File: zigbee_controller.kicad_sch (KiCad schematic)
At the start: 83 parts, among them J1 Terminal MKDS, J10 Terminal MKDS, J11 Terminal MKDS, J12 Terminal MKDS, J13 Terminal MKDS, J2 Conn_01x02, J3 Conn_01x06, J4 Conn_01x07, J5 Conn_01x05, P1 USB_C_Receptacle_GCT_USB4105, Q2 IRLB3813, Q3 IRLB3813, Q4 IRLB3813, Q5 IRLB3813, Q6 IRLB3813, SW2 EN, SW4 Boot, U1 TPS54560, U2 ESP32-C6-MINI-1, U4 TC4427, U5 TC4427, U6 RT9080, U9 CH224K

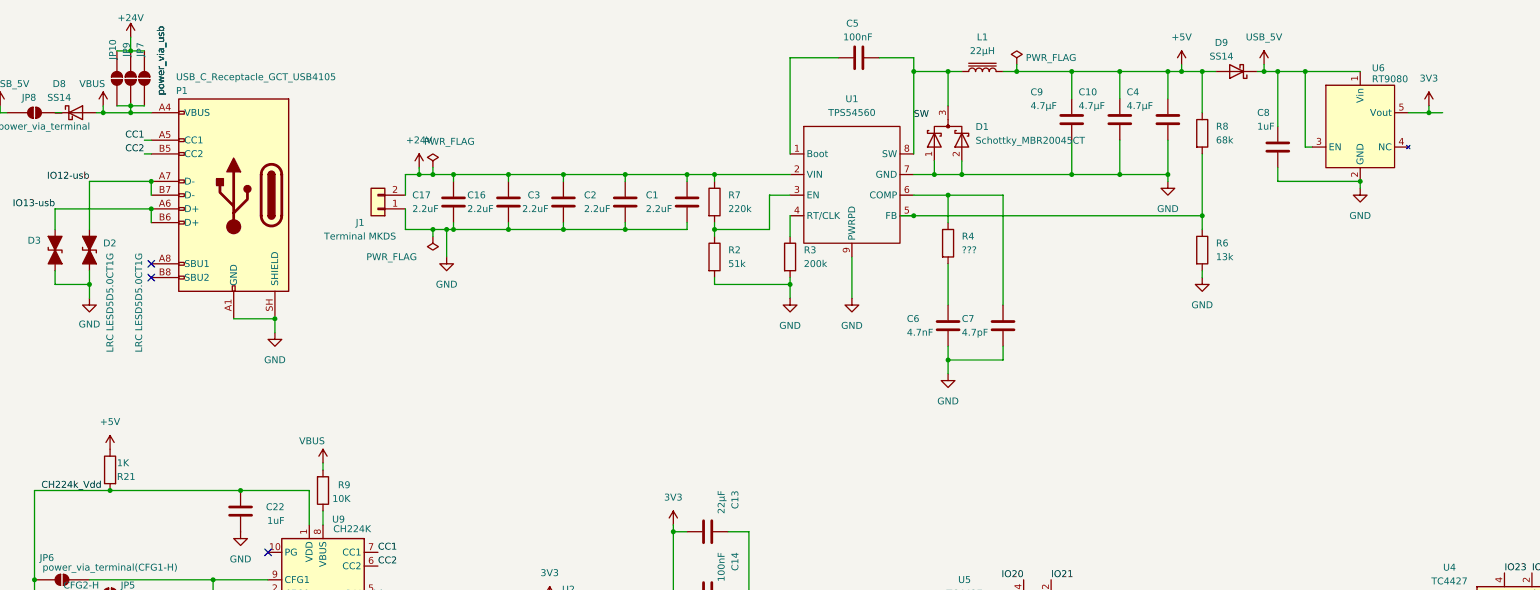
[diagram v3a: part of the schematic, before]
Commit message: USB power, all checks pass
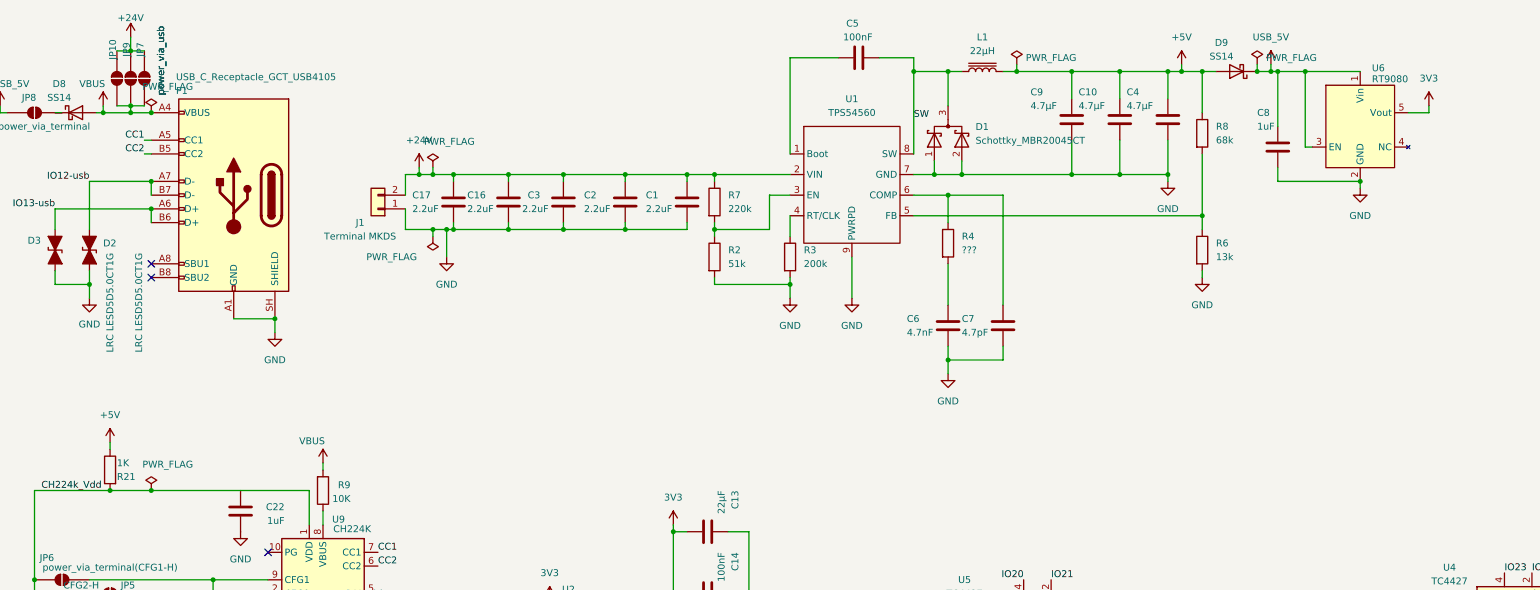
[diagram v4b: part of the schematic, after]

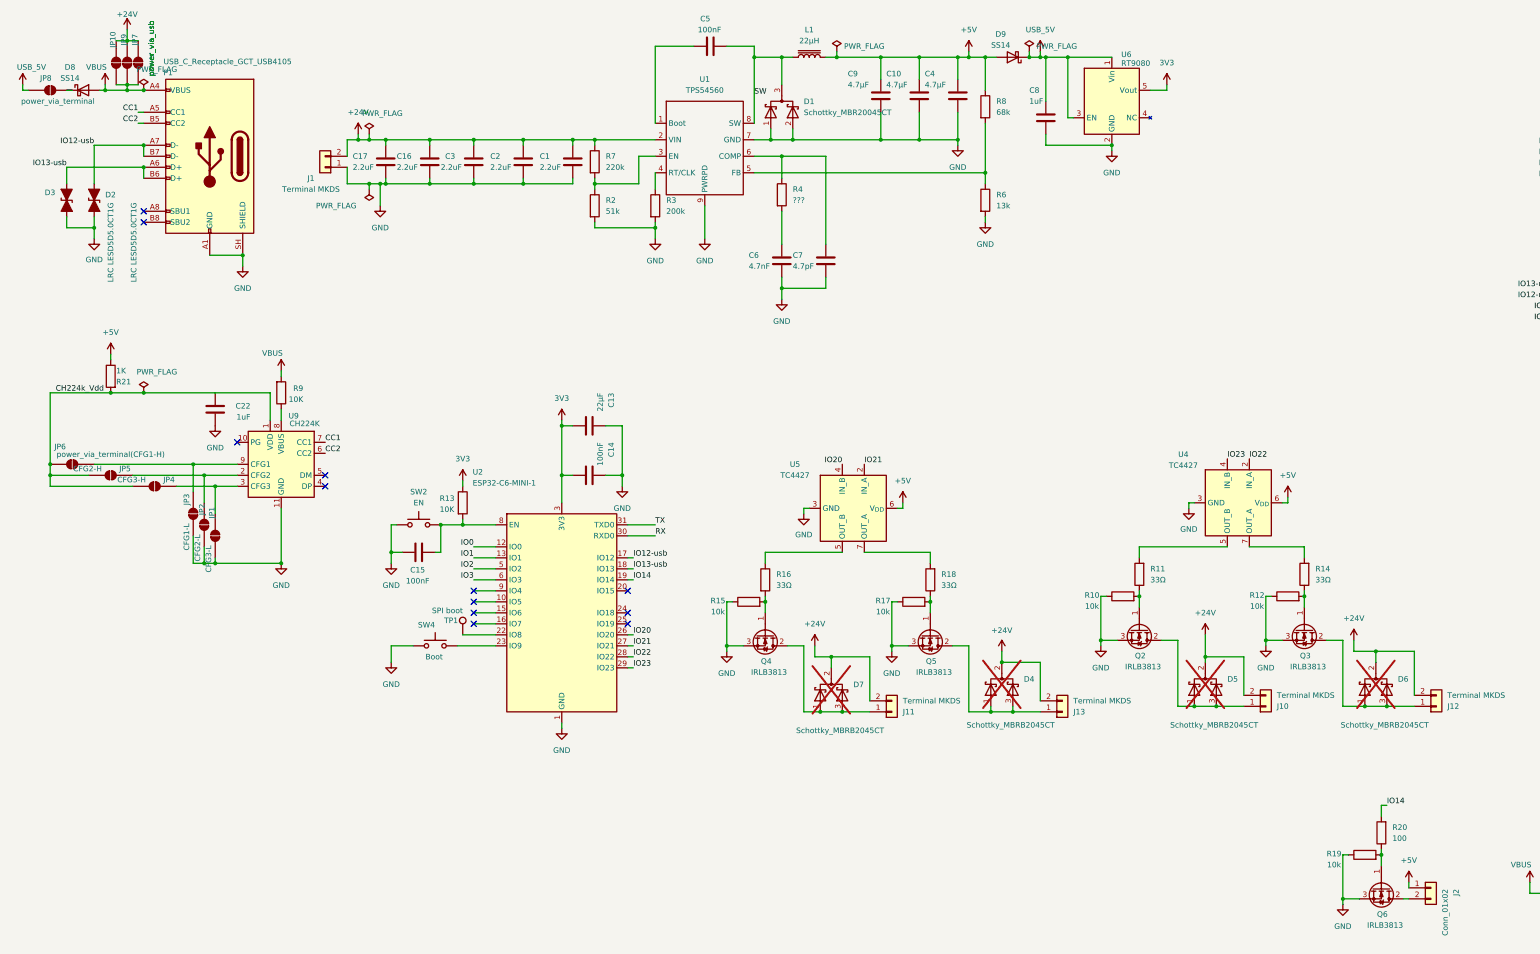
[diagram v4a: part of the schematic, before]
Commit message: changed buck-converter: Inductor, diode, capacitors and resister values
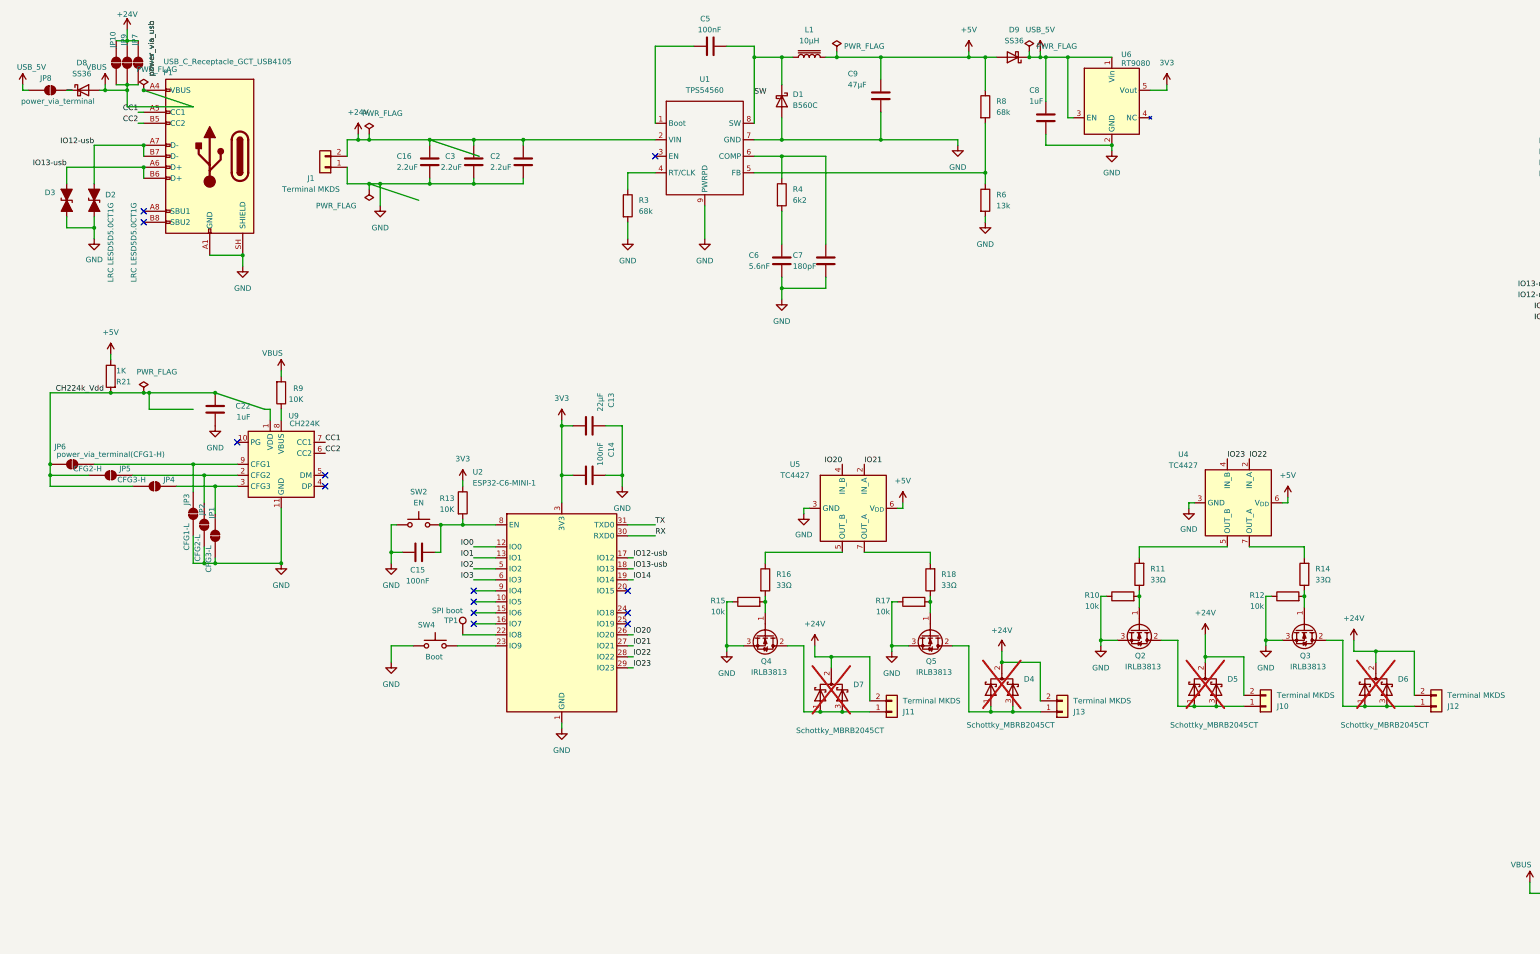
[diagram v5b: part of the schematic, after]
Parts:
- removed C1, C17: 2.2uF, Capacitor_SMD:C_1206_3216Metric_Pad1.33x1.80mm_HandSolder, symbol Device:C
- removed C10, C4: 4.7μF, Capacitor_SMD:C_1206_3216Metric_Pad1.33x1.80mm_HandSolder, symbol Device:C
- removed D1: Schottky_MBR20045CT, Package_TO_SOT_THT:TO-220-3_Vertical, symbol Device:D_Schottky_Dual_CommonCathode_AAK_Parallel
- removed D8, D9: SS14, Diode_SMD:D_SMA, symbol Diode:SS14
- removed J2: Conn_01x02, Connector_JST:JST_XH_B2B-XH-A_1x02_P2.50mm_Vertical, symbol Connector_Generic:Conn_01x02
- removed Q6: IRLB3813, Package_TO_SOT_THT:TO-220-3_Vertical, symbol Transistor_FET:IRLB8721PBF
- removed R19: 10k, Resistor_SMD:R_1206_3216Metric_Pad1.30x1.75mm_HandSolder, symbol Device:R
- removed R2: 51k, Resistor_SMD:R_1206_3216Metric, symbol Device:R
- removed R20: 100, Resistor_SMD:R_1206_3216Metric_Pad1.30x1.75mm_HandSolder, symbol Device:R
- removed R7: 220k, Resistor_SMD:R_1206_3216Metric, symbol Device:R
- added D1: B560C, Diode_SMD:D_SMC, symbol Device:D_Schottky
- added D8, D9: SS36, Diode_SMD:D_SMA, symbol Diode:SS36
- C13, C14, C16, C2, C3: footprint Capacitor_SMD:C_1206_3216Metric_Pad1.33x1.80mm_HandSolder -> Capacitor_SMD:C_1206_3216Metric
- C6: value 4.7nF -> 5.6nF
- C7: value 4.7pF -> 180pF
- C9: value 4.7μF -> 47μF; footprint Capacitor_SMD:C_1206_3216Metric_Pad1.33x1.80mm_HandSolder -> Capacitor_SMD:C_1206_3216Metric
- L1: value 22μH -> 10μH; footprint Inductor_SMD:L_Chilisin_BMRF00101040 -> Inductor_SMD:L_Sunlord_MWSA0503S
- R3: value 200k -> 68k
- R4: value ??? -> 6k2
- R8: footprint Resistor_SMD:R_1206_3216Metric_Pad1.30x1.75mm_HandSolder -> Resistor_SMD:R_1206_3216Metric
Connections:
- net +5V: now also D9.2 (A)
- net GND: now also D1.2 (A)
- net SW: now also D1.1 (K)
- net USB_5V: now also D9.1 (K)
- net VBUS: now also D8.2 (A)
- net at JP8.1 (A): now also D8.1 (K)
- no-connect marks 12 -> 13
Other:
- moved on the sheet: R3

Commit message: final
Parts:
- removed TP4: VBUS, TestPoint:TestPoint_Pad_D2.0mm, symbol Connector:TestPoint
- added TP5: GND, TestPoint:TestPoint_Pad_D2.0mm, symbol Connector:TestPoint
- C15, C22: footprint Capacitor_SMD:C_1206_3216Metric_Pad1.33x1.80mm_HandSolder -> Capacitor_SMD:C_1206_3216Metric
- D2, D3: value LRC LESD5D5.0CT1G -> LESD5D5.0CT1G
- D4, D5, D6, D7: value Schottky_MBRB2045CT -> MBRB2045CT
- R10, R12, R13, R15, R17, R21, R9: footprint Resistor_SMD:R_1206_3216Metric_Pad1.30x1.75mm_HandSolder -> Resistor_SMD:R_1206_3216Metric
- R11, R14, R16, R18: value 33Ω -> 33; footprint Resistor_SMD:R_1206_3216Metric_Pad1.30x1.75mm_HandSolder -> Resistor_SMD:R_1206_3216Metric
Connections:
- net GND: now also TP5.1
